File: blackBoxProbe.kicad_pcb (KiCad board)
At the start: 4 copper layers, 44 x 29 mm, 81 parts, among them J1 USB-ID, J2 JTAG_2X05, J3 JTAG_2X05, J4 Conn_01x04, Q1 Q_NMOS_DUAL, Q2 Q_PMOS_DUAL, U1 MCP1702-MB, U2 USBLC6-2, U3 STM32F103CBT, U4 74X2T45, U5 74X2T45, U6 74X2T45, U7 74X2T45, Y1 Crystal

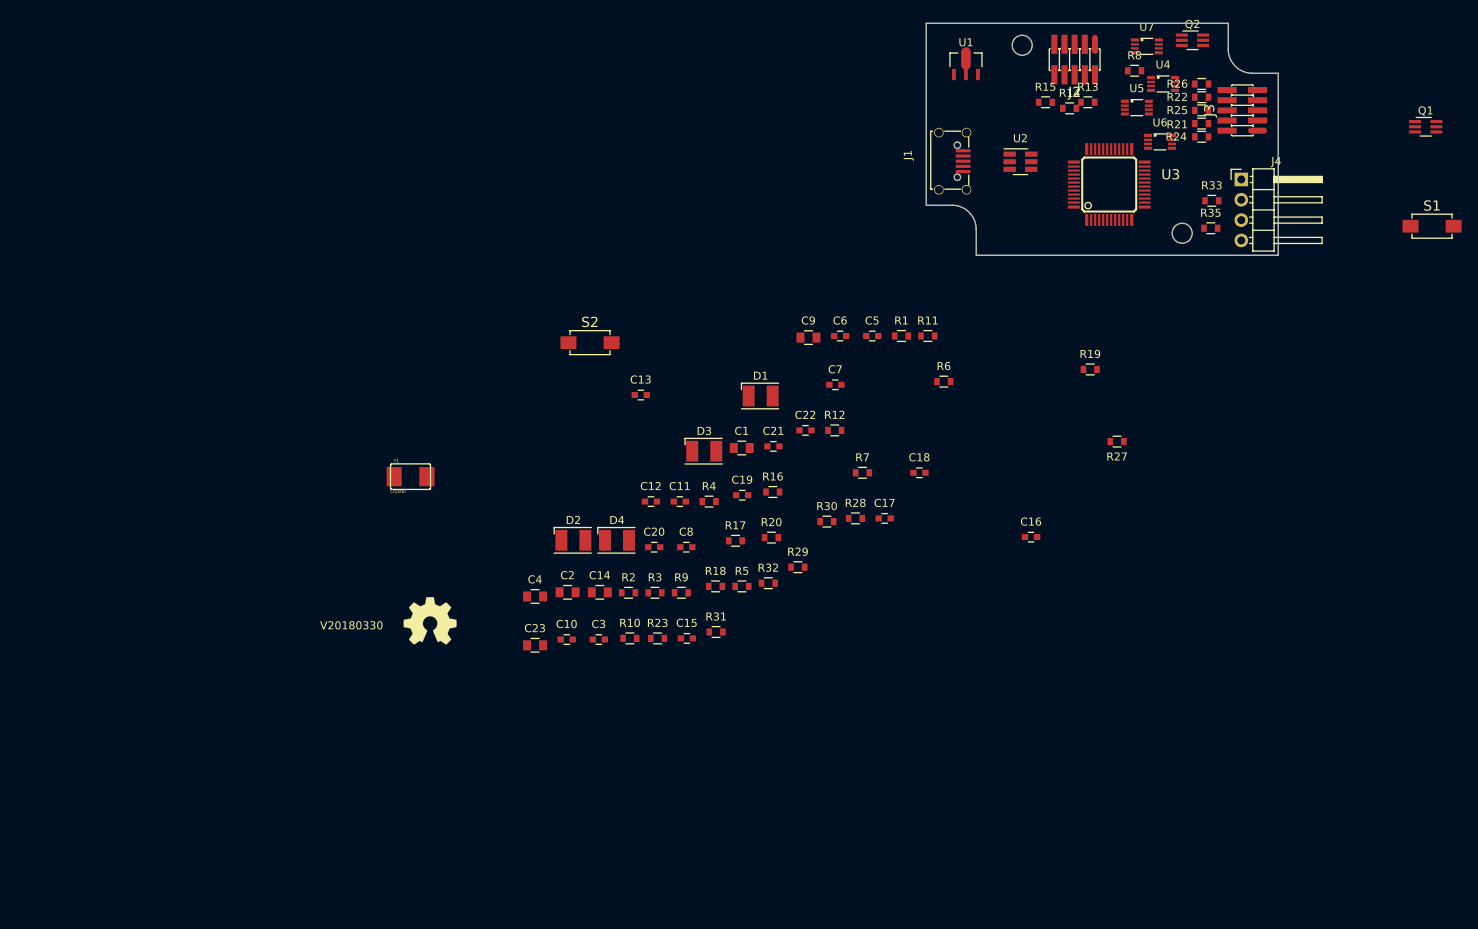
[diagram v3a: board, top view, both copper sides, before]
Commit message: WIP: Switching to bigger case
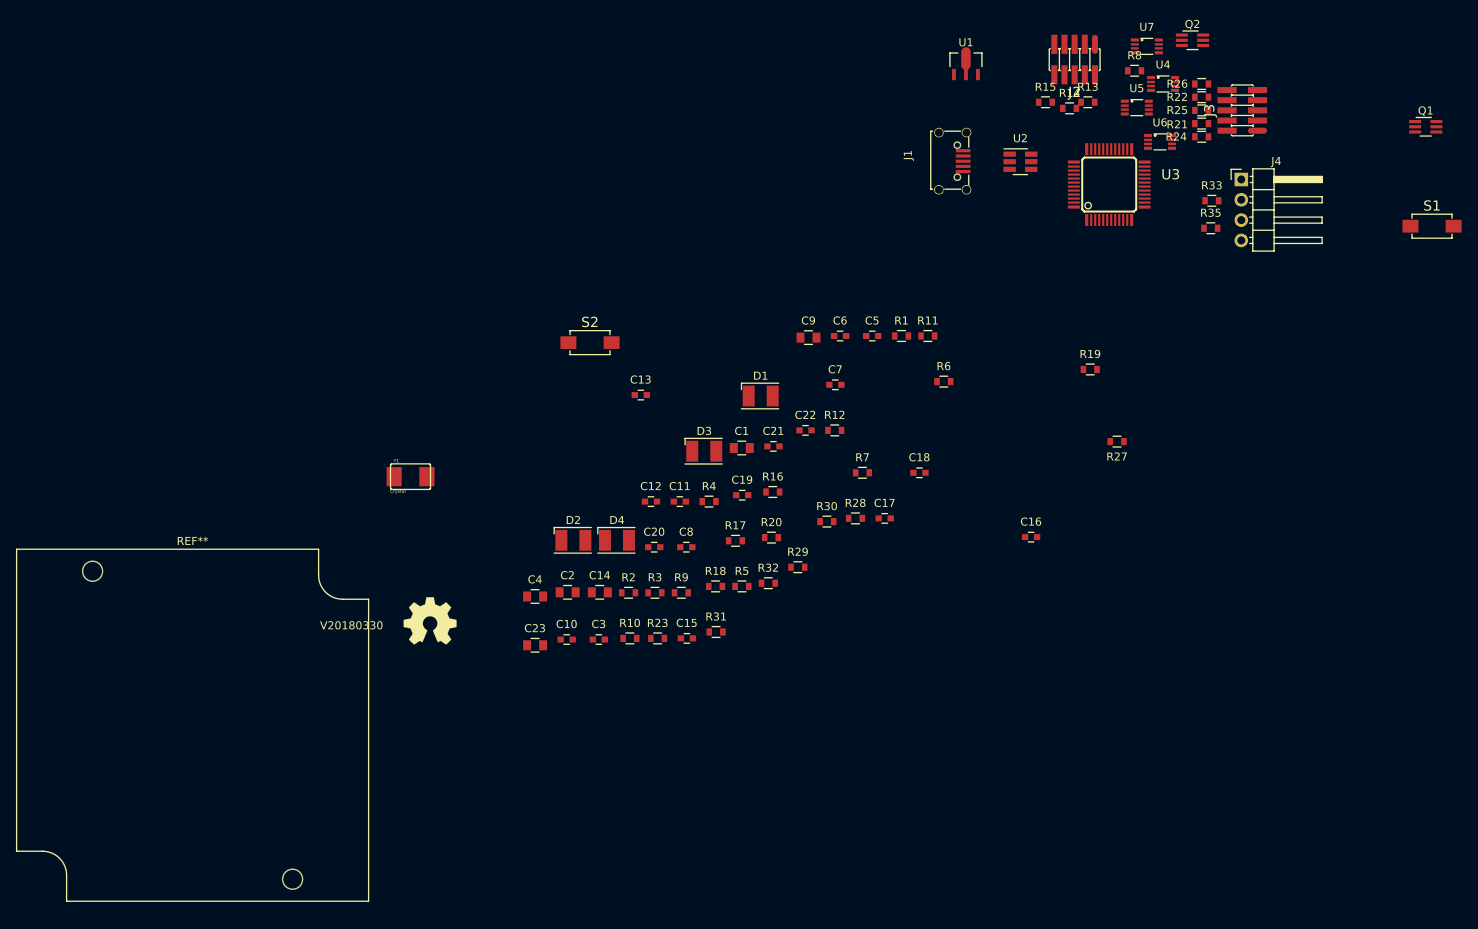
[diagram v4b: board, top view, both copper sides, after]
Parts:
- added REF**: Hammond_1551R, SquantorPcbOutline:Hammond_1551R, F.Cu at (36.3, 173.2)
- moved H2 137.4 mm to (48.8, 192.5)
- moved H1 133.5 mm to (23.8, 154.0)
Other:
- board outline removed
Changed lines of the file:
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@@
 (kicad_pcb (version 4) (host pcbnew 4.0.7-e2-6376~61~ubuntu18.04.1)
   (general
-    (links 187)
+    (links 0)
     (no_connects 187)
-    (area 127.924999 85.424999 172.075001 114.575001)
+    (area 51.816 84.348 199.190187 166.357)
     (thickness 1.6)
-    (drawings 10)
+    (drawings 0)
     (tracks 0)
     (zones 0)
-    (modules 81)
+    (modules 82)
     (nets 76)
   )
@@
   )
   (module SquantorPcbOutline:MountingHole_2.5mm_no_metal locked (layer F.Cu)
-    (at 140 88.25)
+    (at 23.8 154)
     (fp_text reference H1 (at 0 -3) (layer F.SilkS) hide
       (effects (font (size 1 1) (thickness 0.15)))
@@
   )
   (module SquantorPcbOutline:MountingHole_2.5mm_no_metal locked (layer F.Cu)
-    (at 160 111.75)
+    (at 48.8 192.5)
     (fp_text reference H2 (at 0 -3) (layer F.SilkS) hide
       (effects (font (size 1 1) (thickness 0.15)))
@@
       (net 9 "Net-(C13-Pad1)"))
   )
-  (gr_line (start 165.75 88.75) (end 165.75 85.5) (layer Edge.Cuts) (width 0.15))
-  (gr_line (start 172 91.75) (end 168.75 91.75) (layer Edge.Cuts) (width 0.15))
-  (gr_arc (start 168.75 88.75) (end 168.75 91.75) (angle 90) (layer Edge.Cuts) (width 0.15))
-  (gr_line (start 134.25 111.25) (end 134.25 114.5) (layer Edge.Cuts) (width 0.15))
-  (gr_line (start 128 108.25) (end 131.25 108.25) (layer Edge.Cuts) (width 0.15))
-  (gr_arc (start 131.25 111.25) (end 131.25 108.25) (angle 90) (layer Edge.Cuts) (width 0.15))
-  (gr_line (start 128 85.5) (end 128 108.25) (layer Edge.Cuts) (width 0.15))
-  (gr_line (start 165.75 85.5) (end 128 85.5) (layer Edge.Cuts) (width 0.15))
-  (gr_line (start 172 114.5) (end 172 91.75) (layer Edge.Cuts) (width 0.15))
-  (gr_line (start 134.25 114.5) (end 172 114.5) (layer Edge.Cuts) (width 0.15))
+  (module SquantorPcbOutline:Hammond_1551R (layer F.Cu)
+    (at 36.3 173.25)
+    (fp_text reference REF** (at 0 -23) (layer F.SilkS)
+      (effects (font (size 1 1) (thickness 0.15)))
+    )
+    (fp_text value Hammond_1551R (at 0 23) (layer F.Fab)
+      (effects (font (size 1 1) (thickness 0.15)))
+    )
+    (fp_line (start 18.75 -15.75) (end 22 -15.75) (layer F.SilkS) (width 0.05))
+    (fp_line (start 15.75 -22) (end 15.75 -18.75) (layer F.SilkS) (width 0.05))
+    (fp_line (start -15.75 18.75) (end -15.75 22) (layer F.SilkS) (width 0.05))
+    (fp_line (start -22 15.75) (end -18.75 15.75) (layer F.SilkS) (width 0.05))
+    (fp_arc (start -18.75 18.75) (end -18.75 15.75) (angle 90) (layer F.SilkS) (width 0.05))
+    (fp_arc (start 18.75 -18.75) (end 18.75 -15.75) (angle 90) (layer F.SilkS) (width 0.05))
+    (fp_line (start 22 22) (end 22 -15.75) (layer F.SilkS) (width 0.05))
+    (fp_line (start -22 -22) (end 15.75 -22) (layer F.SilkS) (width 0.05))
+    (fp_line (start -22 15.75) (end -22 -22) (layer F.SilkS) (width 0.05))
+    (fp_line (start -15.75 22) (end 22 22) (layer F.SilkS) (width 0.05))
+    (pad 1 thru_hole circle (at -12.5 -19.25) (size 2.5 2.5) (drill 2.5) (layers *.Cu *.Mask))
+    (pad 2 thru_hole circle (at 12.5 19.25) (size 2.5 2.5) (drill 2.5) (layers *.Cu *.Mask))
+  )
 )

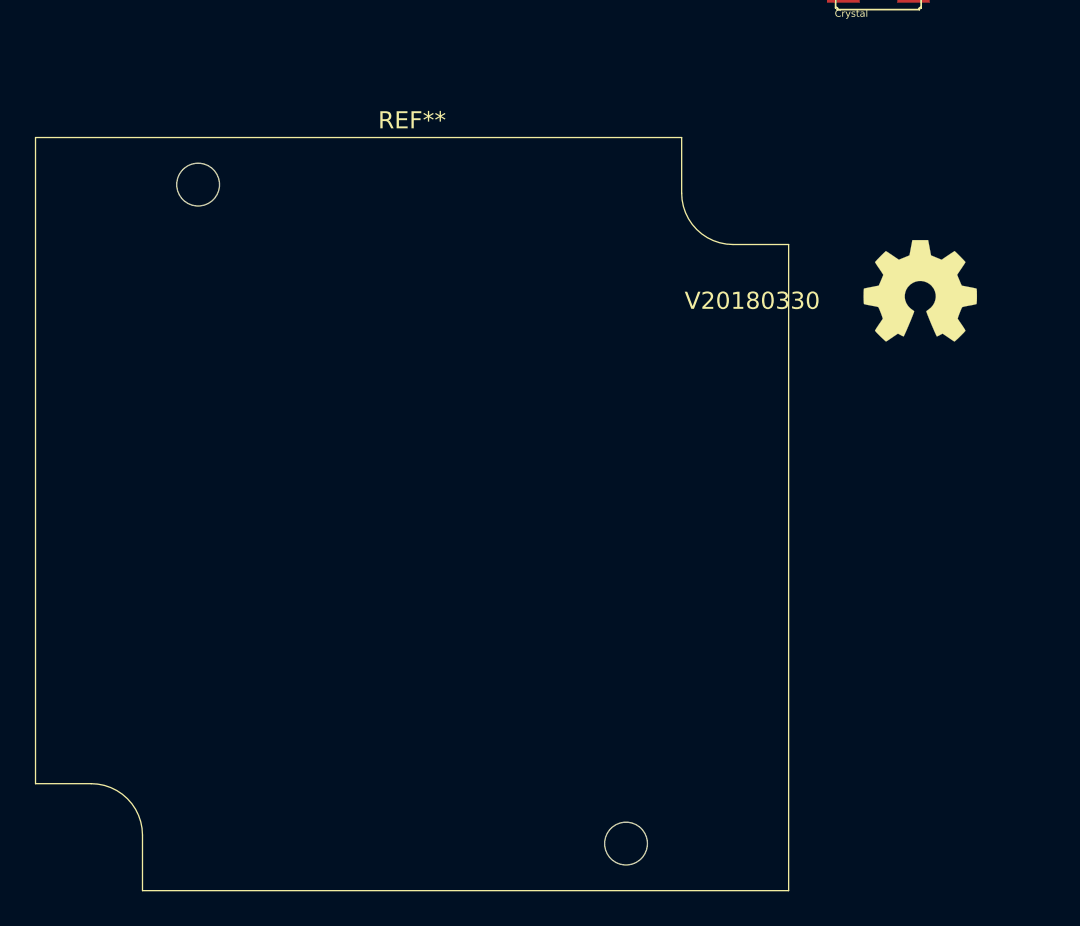
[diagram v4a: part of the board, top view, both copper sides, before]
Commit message: DONE: switched to new PCB layout WIP: rough component placement
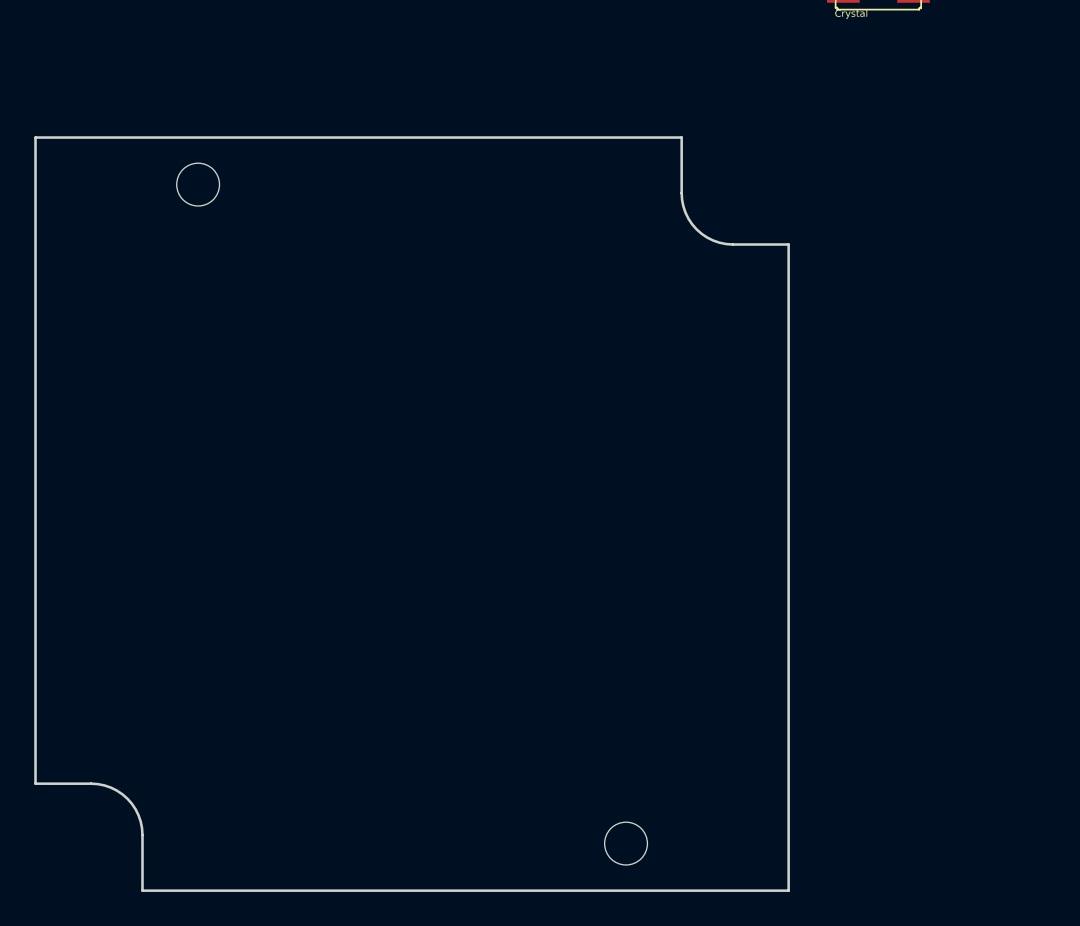
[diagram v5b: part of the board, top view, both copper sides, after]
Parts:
- removed REF**: Hammond_1551R, SquantorPcbOutline:Hammond_1551R
- N1: moved to B.Cu
- moved N1 50.0 mm to (25.6, 189.6), turned to 180 degrees
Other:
- board outline added: 44 x 44 mm

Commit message: WIP: initial placement of all the components, start the tetris music!
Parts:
- moved S1 177.9 mm to (33.2, 192.7)
- moved R8 158.5 mm to (24.2, 182.3)
- moved J2 158.1 mm to (19.2, 183.6), turned to 270 degrees
- moved Q1 157.4 mm to (53.4, 175.8), turned to 180 degrees
- moved R13 150.5 mm to (24.2, 180.7)
- moved R15 150.1 mm to (24.2, 187.3)
- moved R14 150.1 mm to (24.2, 184.0)
- moved Q2 142.2 mm to (53.4, 180.3)
- moved U7 141.6 mm to (47.5, 179.8)
- moved R19 139.8 mm to (18.1, 179.3), turned to 180 degrees
- moved J4 139.5 mm to (53.4, 185.3)
- moved R33 139.1 mm to (50.0, 187.9), turned to 180 degrees
- moved R35 138.0 mm to (50.0, 189.5), turned to 180 degrees
- moved U2 135.3 mm to (22.9, 171.0)
- moved U3 133.8 mm to (33.4, 169.7), turned to 90 degrees
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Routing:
- net Net-(C2-Pad2): track 0.00 -> 16.2 mm
- net GND: track 0.00 -> 11.7 mm, vias 0 -> 2
- net +3V3: track 0.00 -> 7.14 mm, vias 0 -> 1
- added copper zone on In2.Cu, net +3V3
- added copper zone on F.Cu, net +5V
- added copper zone on In1.Cu, net GND
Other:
- rule pad_to_mask_clearance: 0.2 -> 0.1

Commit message: DONE: netlist updates
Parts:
- removed C10: 100n, SquantorRcl:C_0603
- Y1: value Crystal -> 8.000MHz
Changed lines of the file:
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@@
 (kicad_pcb (version 4) (host pcbnew 4.0.7-e2-6376~61~ubuntu18.04.1)
   (general
-    (links 187)
-    (no_connects 186)
-    (area 14.147999 84.682 199.190187 197.252)
+    (links 185)
+    (no_connects 174)
+    (area 14.224999 151.174999 58.375001 195.325001)
     (thickness 1.6)
     (drawings 10)
     (tracks 27)
     (zones 0)
-    (modules 81)
+    (modules 80)
     (nets 76)
   )
@@
   )
   (module SquantorRcl:C_0603 (layer F.Cu)
-    (at 17.25 165.125)
-    (descr "Capacitor SMD 0603, reflow soldering, AVX (see smccp.pdf)")
-    (tags "capacitor 0603")
-    (attr smd)
-    (fp_text reference C10 (at 0 -1.9) (layer F.SilkS)
-      (effects (font (size 1 1) (thickness 0.15)))
-    )
-    (fp_text value 100n (at 0 1.9) (layer F.Fab)
-      (effects (font (size 1 1) (thickness 0.15)))
-    )
-    (fp_line (start -0.8 0.4) (end -0.8 -0.4) (layer F.Fab) (width 0.15))
-    (fp_line (start 0.8 0.4) (end -0.8 0.4) (layer F.Fab) (width 0.15))
-    (fp_line (start 0.8 -0.4) (end 0.8 0.4) (layer F.Fab) (width 0.15))
-    (fp_line (start -0.8 -0.4) (end 0.8 -0.4) (layer F.Fab) (width 0.15))
-    (fp_line (start -1.45 -0.75) (end 1.45 -0.75) (layer F.CrtYd) (width 0.05))
-    (fp_line (start -1.45 0.75) (end 1.45 0.75) (layer F.CrtYd) (width 0.05))
-    (fp_line (start -1.45 -0.75) (end -1.45 0.75) (layer F.CrtYd) (width 0.05))
-    (fp_line (start 1.45 -0.75) (end 1.45 0.75) (layer F.CrtYd) (width 0.05))
-    (fp_line (start -0.35 -0.6) (end 0.35 -0.6) (layer F.SilkS) (width 0.15))
-    (fp_line (start 0.35 0.6) (end -0.35 0.6) (layer F.SilkS) (width 0.15))
-    (pad 1 smd rect (at -0.75 0) (size 0.8 0.75) (layers F.Cu F.Paste F.Mask)
-      (net 1 +5V))
-    (pad 2 smd rect (at 0.75 0) (size 0.8 0.75) (layers F.Cu F.Paste F.Mask)
-      (net 2 GND))
-    (model Capacitors_SMD.3dshapes/C_0603.wrl
-      (at (xyz 0 0 0))
-      (scale (xyz 1 1 1))
-      (rotate (xyz 0 0 0))
-    )
-  )
-  (module SquantorRcl:C_0603 (layer F.Cu)
     (at 56.125 171.05 90)
     (descr "Capacitor SMD 0603, reflow soldering, AVX (see smccp.pdf)")
@@
       (effects (font (size 0.4064 0.4064) (thickness 0.0254)))
     )
-    (fp_text value Crystal (at -1.5748 1.8288 90) (layer F.SilkS)
+    (fp_text value 8.000MHz (at -1.5748 1.8288 90) (layer F.SilkS)
       (effects (font (size 0.4064 0.4064) (thickness 0.0254)))
     )

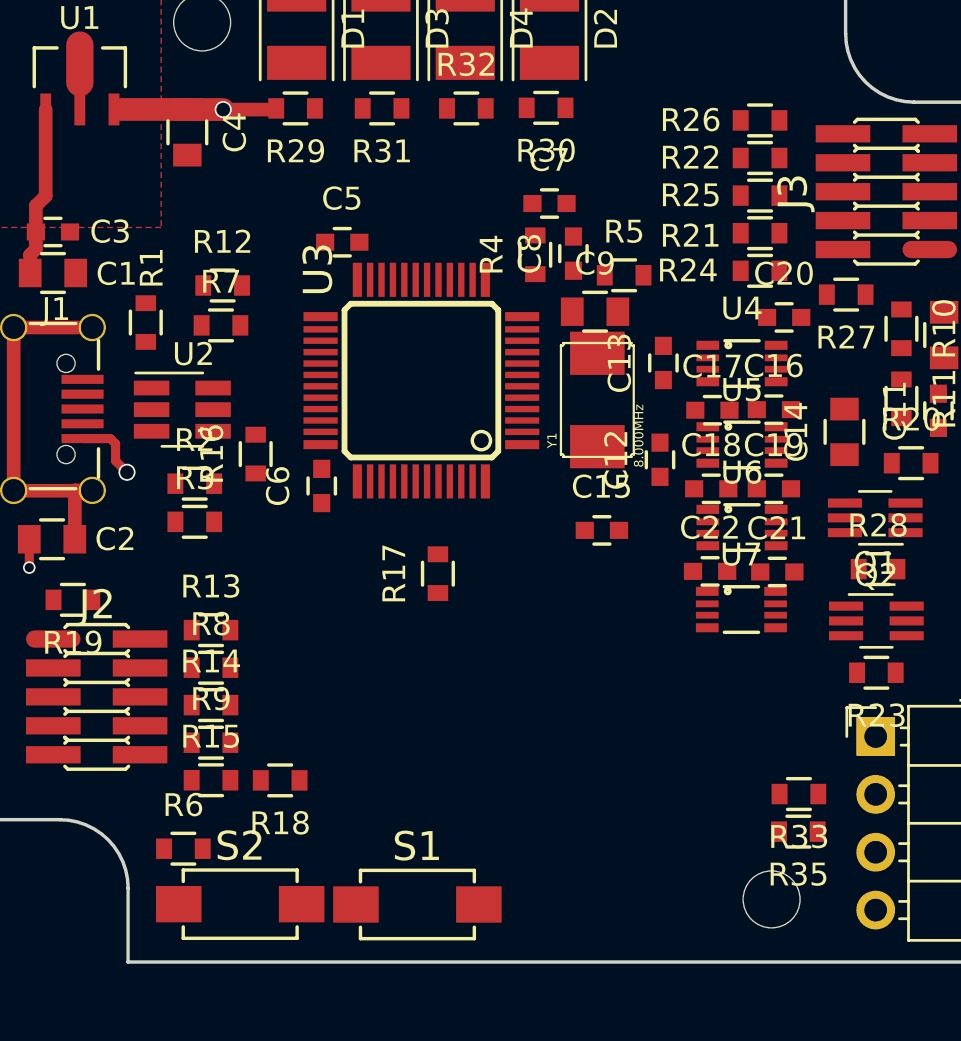
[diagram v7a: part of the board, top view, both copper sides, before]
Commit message: FIX: fixed boot0 pulldown to something stronger WIP: further component placement WIP: need to replace JTAG headers to TH headers
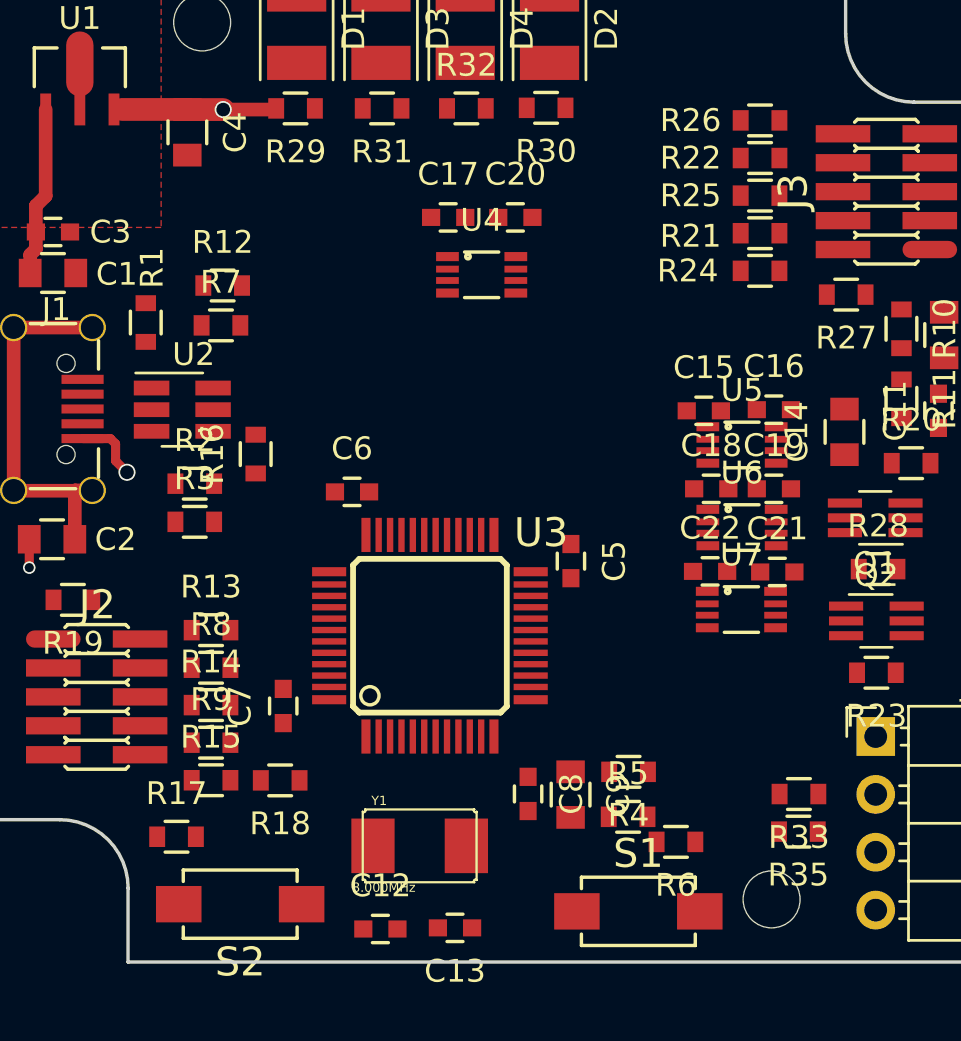
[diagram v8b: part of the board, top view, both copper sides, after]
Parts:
- moved C13 26.4 mm to (34.9, 193.8), turned to 180 degrees
- moved C7 25.0 mm to (27.4, 184.0), turned to 90 degrees
- moved C12 24.0 mm to (31.6, 193.8), turned to 0 degrees
- moved C8 23.8 mm to (38.1, 187.9), turned to 270 degrees
- moved R5 23.8 mm to (42.5, 188.9)
- moved R4 23.1 mm to (42.5, 186.9), turned to 180 degrees
- moved R6 21.6 mm to (44.6, 190.0), turned to 180 degrees
- moved C9 21.2 mm to (40.0, 187.9), turned to 270 degrees
- moved Y1 21.1 mm to (33.4, 190.2), turned to 0 degrees
- moved C5 17.2 mm to (40.0, 177.7), turned to 270 degrees
- moved R17 16.3 mm to (22.7, 189.8), turned to 0 degrees
- moved C17 14.4 mm to (34.6, 162.6)
- moved C20 12.6 mm to (37.5, 162.6)
- moved U4 12.1 mm to (36.1, 165.1)
- moved U3 11.2 mm to (33.8, 180.9), turned to 0 degrees
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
